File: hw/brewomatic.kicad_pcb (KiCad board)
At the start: 2 copper layers, 95.2 x 70.1 mm, 36 parts, among them J1 CON_MAX31865, J10 TP_MOC, J11 FAN, J2 EXP1, J3 EXP2, J4 12V_IN, J5 230V_CONN, J6 HEATING_CONN, J7 PUMP_CONN, J8 12V_ALIM_CONN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

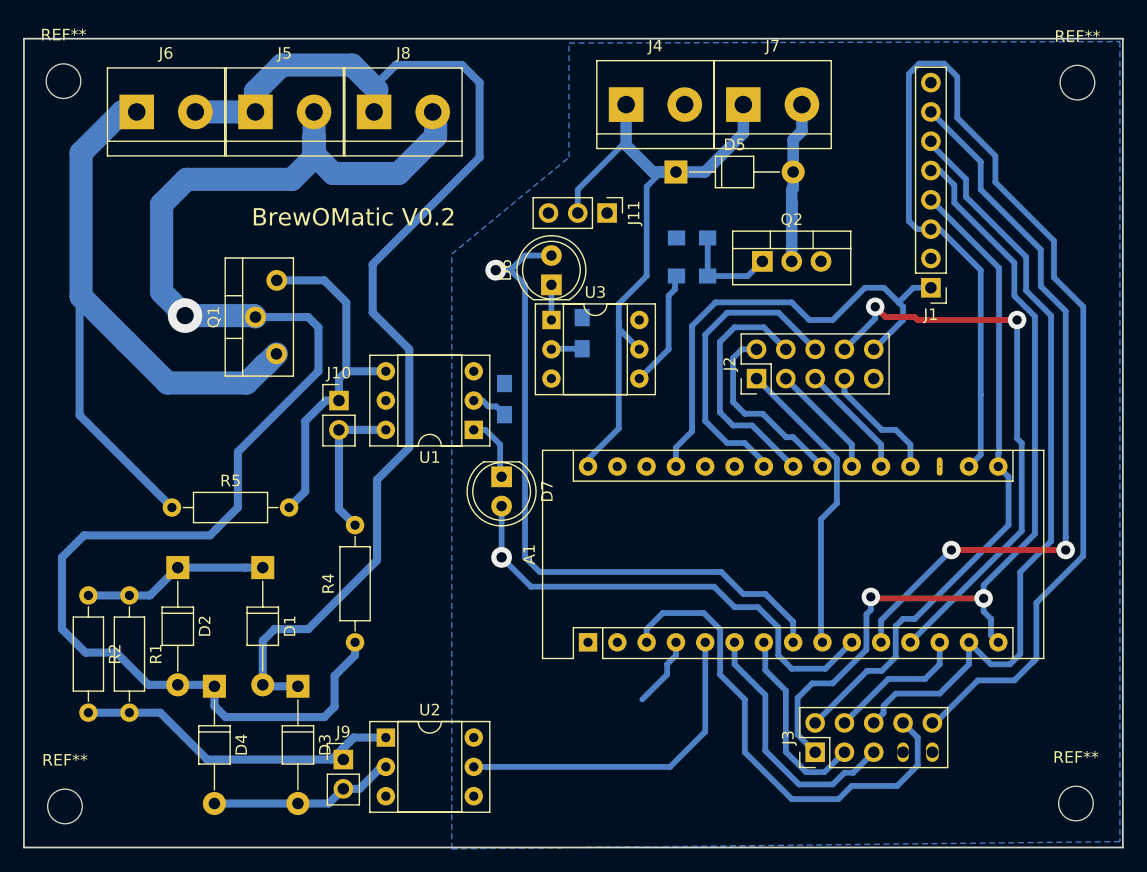
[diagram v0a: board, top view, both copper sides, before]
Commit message: hw: Add testpoints for various input/output
This is helpful to plug logic analyzer on them
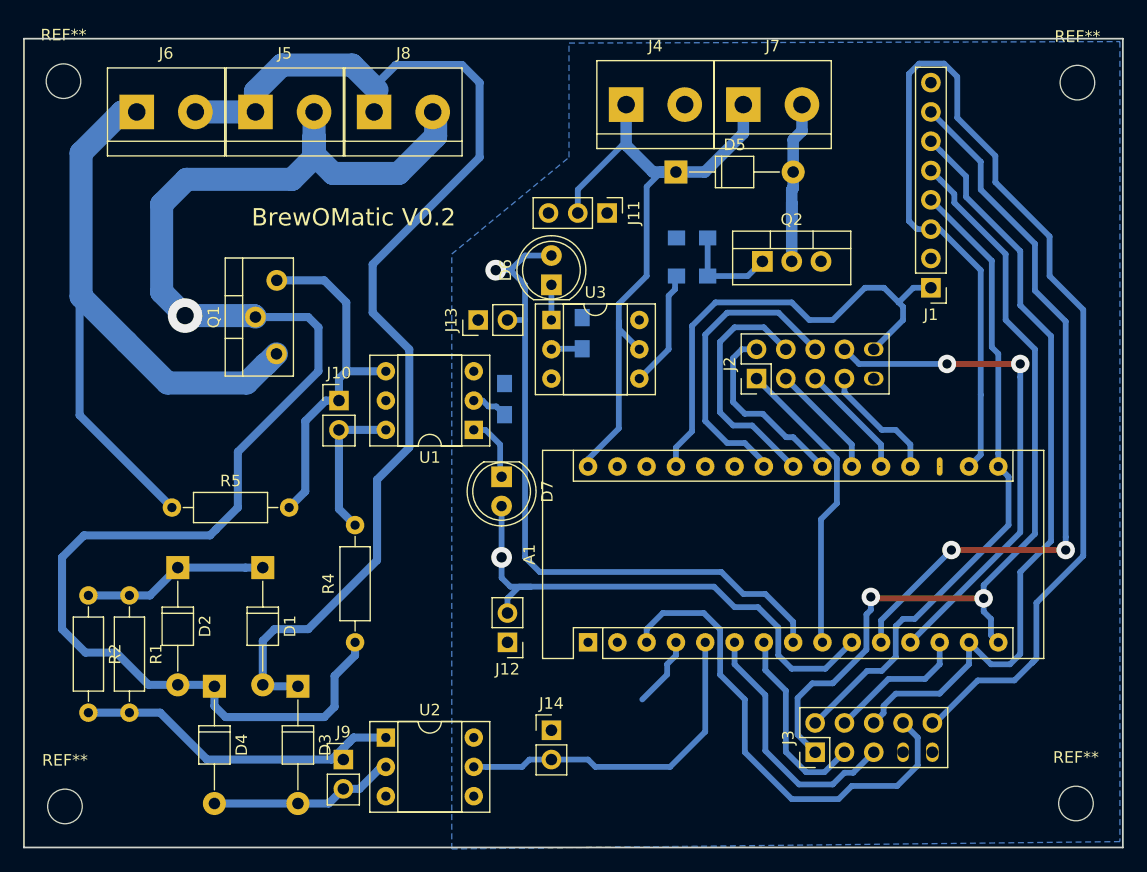
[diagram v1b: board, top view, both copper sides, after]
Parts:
- added J12: TP_TRIAC, Pin_Headers:Pin_Header_Straight_1x02_Pitch2.54mm, F.Cu at (158.8, 139.7)
- added J13: TP_PUMP_CTRL, Pin_Headers:Pin_Header_Straight_1x02_Pitch2.54mm, F.Cu at (156.2, 111.8)
- added J14: TP_ZERO_CROSS, Pin_Headers:Pin_Header_Straight_1x02_Pitch2.54mm, F.Cu at (162.6, 147.3)
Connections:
- J1 pad 2: Net-(J1-Pad2) -> GND
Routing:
- net /LCD7: track 49.7 -> 43.8 mm
- net /TRIAC_CTRL: track 41.2 -> 45.9 mm
- net /PUMP_CTRL: track 58.1 -> 59.6 mm
- net /ZERO_CROSS_INT: track 29.1 -> 29.6 mm
